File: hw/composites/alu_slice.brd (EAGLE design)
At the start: 50 x 50 mm, 7 parts, among them CON2 GENERIC-2X10

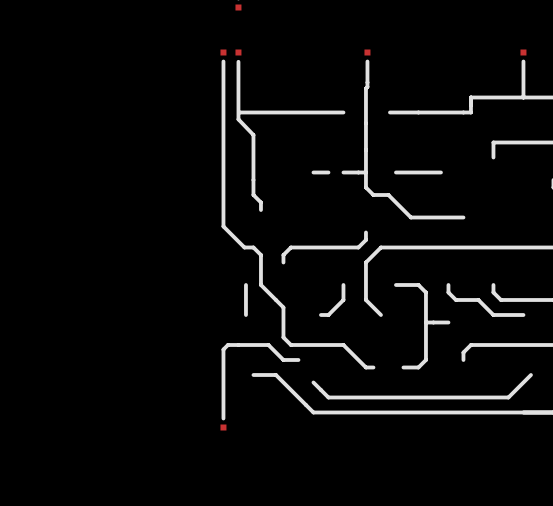
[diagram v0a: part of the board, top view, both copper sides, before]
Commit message: adds support for logical OR
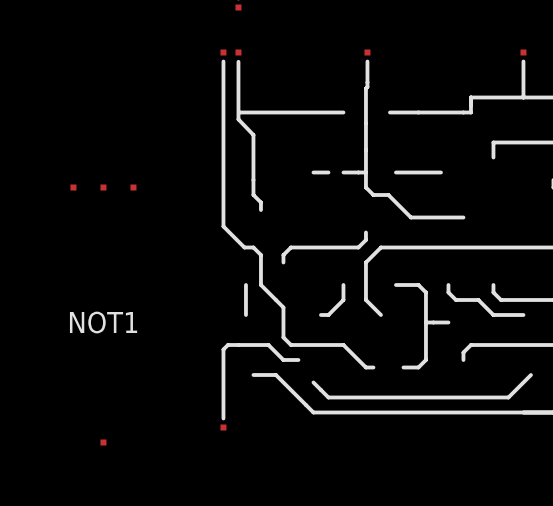
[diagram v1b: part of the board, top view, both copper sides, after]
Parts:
- added NOT1: NOTVERTICAL, p.peter-gator:NOT-VERTICAL
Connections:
- new net N$3: NOT1.NOT, SEL2.I7
- net +5V: now also NOT1._VP
- net GND: now also NOT1._VN
- net NOR: now also NOT1.A; no longer SEL2.I7
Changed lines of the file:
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@@
 <element name="XOR1" library="p.peter-gator" package="XOR" value="XOR" x="0.5" y="-20"/>
 <element name="XOR4" library="p.peter-gator" package="XOR" value="XOR" x="0" y="-34"/>
+<element name="NOT1" library="p.peter-gator" package="NOT-VERTICAL" value="NOTVERTICAL" x="-5.5" y="-34.5"/>
 </elements>
 <signals>
@@
 <contactref element="XOR1" pad="_VP"/>
 <contactref element="XOR4" pad="_VP"/>
+<contactref element="NOT1" pad="_VP"/>
 <wire x1="37.5" y1="34.5" x2="48.5" y2="32" width="0" layer="19" extent="1-1"/>
 <wire x1="15.5" y1="32" x2="37.5" y2="34.5" width="0" layer="19" extent="1-1"/>
 <wire x1="48" y1="5" x2="48.5" y2="32" width="0" layer="19" extent="1-1"/>
-<wire x1="17.07" y1="1.27" x2="48" y2="5" width="0" layer="19" extent="1-16"/>
-<wire x1="1.5" y1="-7.5" x2="17.07" y2="1.27" width="0" layer="19" extent="1-16"/>
+<wire x1="17.07" y1="1.27" x2="15.5" y2="32" width="0" layer="19" extent="1-1"/>
+<wire x1="1.5" y1="-7.5" x2="17.07" y2="1.27" width="0" layer="19" extent="1-1"/>
 <wire x1="1" y1="-21.5" x2="1.5" y2="-7.5" width="0" layer="19" extent="1-1"/>
+<wire x1="-2.5" y1="-26" x2="1" y2="-21.5" width="0" layer="19" extent="1-1"/>
 </signal>
 <signal name="GND">
@@
 <contactref element="XOR1" pad="_VN"/>
 <contactref element="XOR4" pad="_VN"/>
+<contactref element="NOT1" pad="_VN"/>
 <wire x1="27.8" y1="32" x2="47.5" y2="32" width="0" layer="19" extent="1-1"/>
 <wire x1="25.2" y1="34.5" x2="27.8" y2="32" width="0" layer="19" extent="1-1"/>
@@
 <wire x1="13.8" y1="-7.5" x2="39.93" y2="1.27" width="0" layer="19" extent="1-1"/>
 <wire x1="13.3" y1="-21.5" x2="13.8" y2="-7.5" width="0" layer="19" extent="1-1"/>
+<wire x1="-3.5" y1="-26" x2="13.3" y2="-21.5" width="0" layer="19" extent="1-1"/>
 </signal>
 <signal name="NOR">
 <contactref element="XOR2" pad="NOR"/>
-<contactref element="SEL2" pad="I7"/>
-<wire x1="39.8" y1="5" x2="33.2" y2="34.5" width="0" layer="19" extent="1-1"/>
+<contactref element="NOT1" pad="A"/>
+<wire x1="-3.5" y1="-34.5" x2="33.2" y2="34.5" width="0" layer="19" extent="1-1"/>
 </signal>
 <signal name="B">
@@
 <wire x1="27.23" y1="1.27" x2="0.5" y2="-34" width="0" layer="19" extent="1-16"/>
 </signal>
+<signal name="N$3">
+<contactref element="SEL2" pad="I7"/>
+<contactref element="NOT1" pad="NOT"/>
+<wire x1="-4.5" y1="-26" x2="39.8" y2="5" width="0" layer="19" extent="1-1"/>
+</signal>
 </signals>

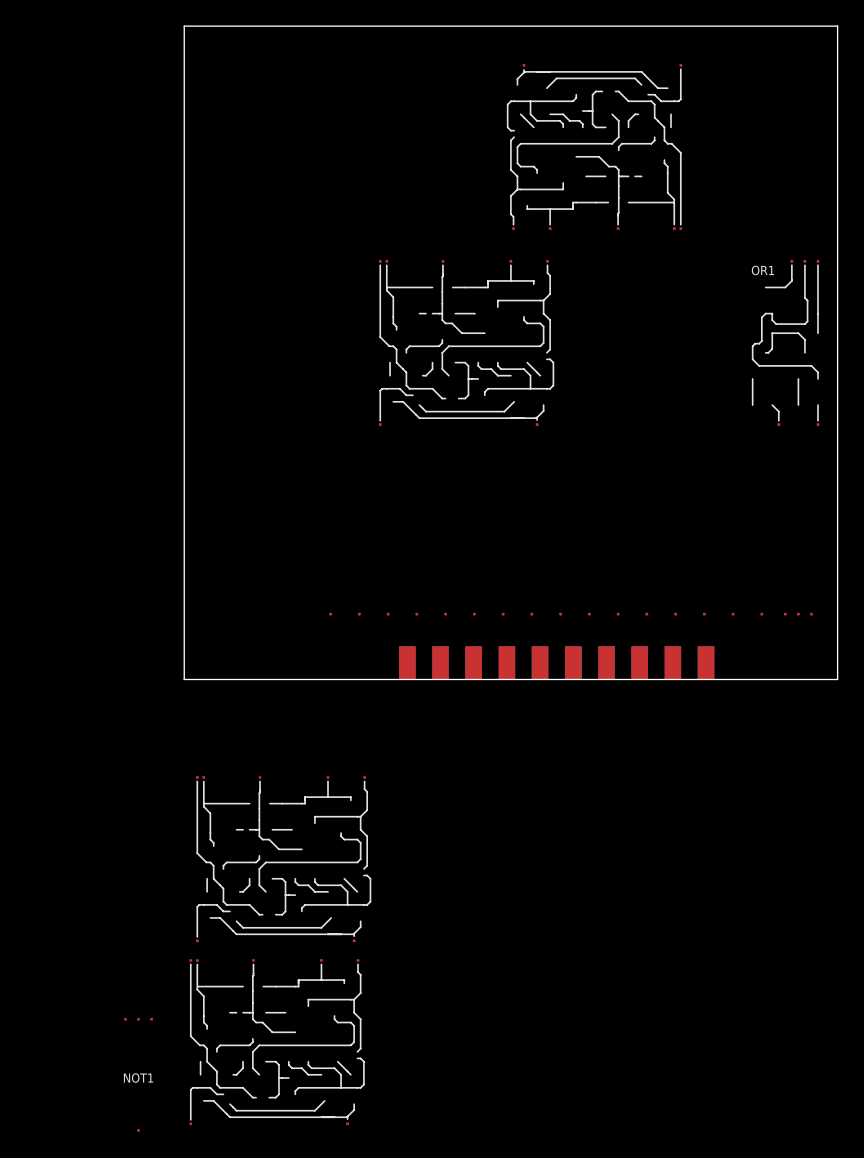
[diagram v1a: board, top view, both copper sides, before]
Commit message: adds support for bit shifts
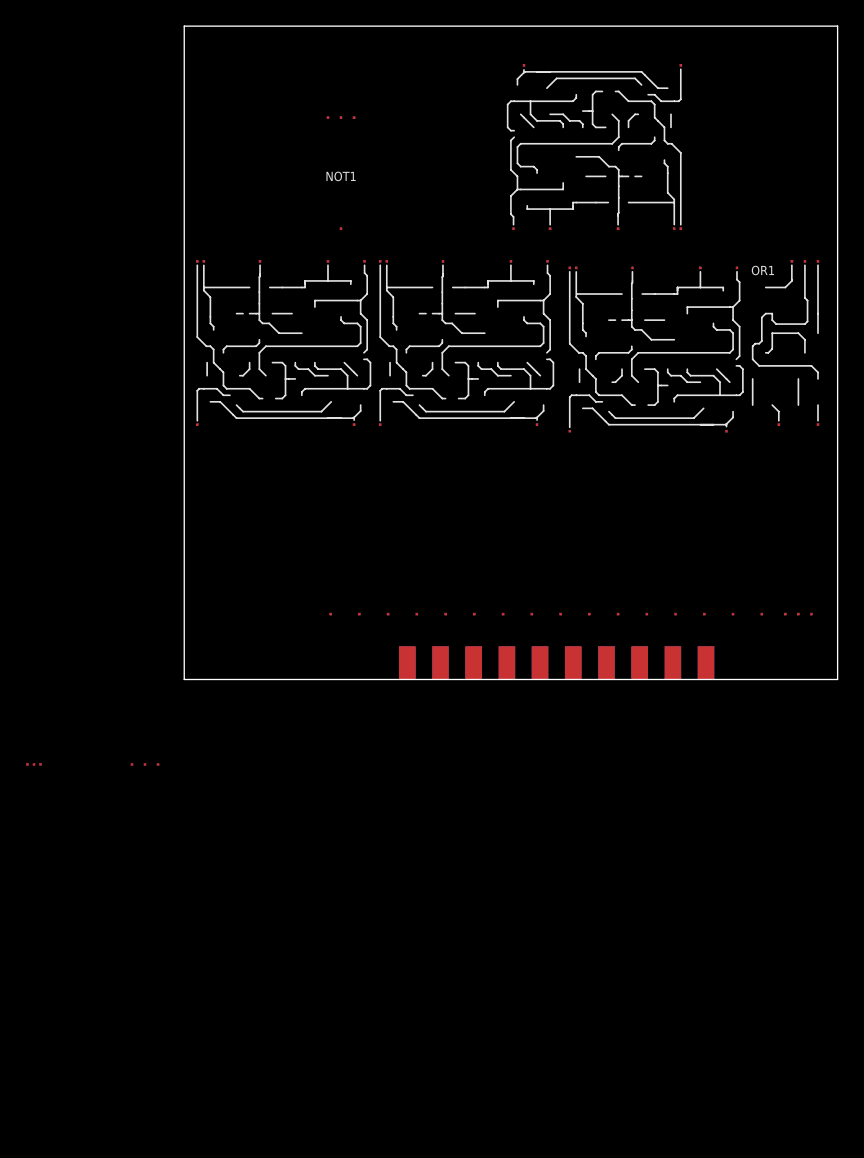
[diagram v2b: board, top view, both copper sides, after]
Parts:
- added SEL1: 1_BIT_SELECT, p.peter-gator:SELECTOR-2-LANE-NOMUX
- moved NOT1 70.7 mm to (10.0, 34.5)
- moved XOR4 60.4 mm to (29.0, 19.0)
- moved XOR1 39.5 mm to (0.50, 19.5)
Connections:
- new net N$5: SEL1.OUT, SEL2.I1
- new net RIGHT_IN: CON2.11, SEL1.A
- net +5V: now also SEL1._VP
- net CARRY_IN: now also SEL1.B
- net GND: now also SEL1._VN
- net LEFT_IN: no longer SEL2.I1
- net NC: no longer CON2.10, CON2.11, CON2.12, CON2.14
- net SUBTRACT: now also SEL1.SEL
- net S_OR: now also CON2.10
- net S_SHIFT: now also CON2.14
- net S_XOR: now also CON2.12
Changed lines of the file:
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@@
 <element name="SEL2" library="p.peter-gator" package="SELECTOR-8_BIT-NOMUX" value="8_BIT_SELECT" x="10" y="5"/>
 <element name="CON2" library="p.peter-connectors" package="PINHEADER-100MIL-2X10-EDGE" value="GENERIC-2X10" x="28.5" y="0"/>
-<element name="XOR1" library="p.peter-gator" package="XOR" value="XOR" x="0.5" y="-20"/>
-<element name="XOR4" library="p.peter-gator" package="XOR" value="XOR" x="0" y="-34"/>
-<element name="NOT1" library="p.peter-gator" package="NOT-VERTICAL" value="NOTVERTICAL" x="-5.5" y="-34.5"/>
+<element name="XOR1" library="p.peter-gator" package="XOR" value="XOR" x="0.5" y="19.5"/>
+<element name="XOR4" library="p.peter-gator" package="XOR" value="XOR" x="29" y="19"/>
+<element name="NOT1" library="p.peter-gator" package="NOT-VERTICAL" value="NOTVERTICAL" x="10" y="34.5"/>
+<element name="SEL1" library="p.peter-gator" package="SELECTOR-2-LANE-NOMUX" value="1_BIT_SELECT" x="-13" y="-6.5"/>
 </elements>
 <signals>
@@
 <contactref element="XOR3" pad="A"/>
 <contactref element="CON2" pad="5"/>
+<contactref element="SEL1" pad="B"/>
 <wire x1="22.15" y1="1.27" x2="27" y2="19.5" width="0" layer="19" extent="1-16"/>
+<wire x1="-11.5" y1="-6.5" x2="22.15" y2="1.27" width="0" layer="19" extent="1-16"/>
 </signal>
 <signal name="SUM">
@@
 <contactref element="XOR4" pad="_VP"/>
 <contactref element="NOT1" pad="_VP"/>
+<contactref element="SEL1" pad="_VP"/>
 <wire x1="37.5" y1="34.5" x2="48.5" y2="32" width="0" layer="19" extent="1-1"/>
-<wire x1="15.5" y1="32" x2="37.5" y2="34.5" width="0" layer="19" extent="1-1"/>
+<wire x1="30" y1="31.5" x2="37.5" y2="34.5" width="0" layer="19" extent="1-1"/>
+<wire x1="15.5" y1="32" x2="30" y2="31.5" width="0" layer="19" extent="1-1"/>
+<wire x1="13" y1="43" x2="15.5" y2="32" width="0" layer="19" extent="1-1"/>
+<wire x1="1.5" y1="32" x2="15.5" y2="32" width="0" layer="19" extent="1-1"/>
 <wire x1="48" y1="5" x2="48.5" y2="32" width="0" layer="19" extent="1-1"/>
 <wire x1="17.07" y1="1.27" x2="15.5" y2="32" width="0" layer="19" extent="1-1"/>
-<wire x1="1.5" y1="-7.5" x2="17.07" y2="1.27" width="0" layer="19" extent="1-1"/>
-<wire x1="1" y1="-21.5" x2="1.5" y2="-7.5" width="0" layer="19" extent="1-1"/>
-<wire x1="-2.5" y1="-26" x2="1" y2="-21.5" width="0" layer="19" extent="1-1"/>
+<wire x1="-2" y1="-6.5" x2="17.07" y2="1.27" width="0" layer="19" extent="1-1"/>
 </signal>
 <signal name="GND">
@@
 <contactref element="XOR4" pad="_VN"/>
 <contactref element="NOT1" pad="_VN"/>
-<wire x1="27.8" y1="32" x2="47.5" y2="32" width="0" layer="19" extent="1-1"/>
+<contactref element="SEL1" pad="_VN"/>
+<wire x1="42.3" y1="31.5" x2="47.5" y2="32" width="0" layer="19" extent="1-1"/>
+<wire x1="27.8" y1="32" x2="42.3" y2="31.5" width="0" layer="19" extent="1-1"/>
 <wire x1="25.2" y1="34.5" x2="27.8" y2="32" width="0" layer="19" extent="1-1"/>
-<wire x1="46" y1="5" x2="47.5" y2="32" width="0" layer="19" extent="1-1"/>
+<wire x1="13.8" y1="32" x2="25.2" y2="34.5" width="0" layer="19" extent="1-1"/>
+<wire x1="12" y1="43" x2="13.8" y2="32" width="0" layer="19" extent="1-1"/>
+<wire x1="46" y1="5" x2="42.3" y2="31.5" width="0" layer="19" extent="1-1"/>
 <wire x1="39.93" y1="1.27" x2="46" y2="5" width="0" layer="19" extent="1-1"/>
-<wire x1="13.8" y1="-7.5" x2="39.93" y2="1.27" width="0" layer="19" extent="1-1"/>
-<wire x1="13.3" y1="-21.5" x2="13.8" y2="-7.5" width="0" layer="19" extent="1-1"/>
-<wire x1="-3.5" y1="-26" x2="13.3" y2="-21.5" width="0" layer="19" extent="1-1"/>
+<wire x1="-4" y1="-6.5" x2="13.8" y2="32" width="0" layer="19" extent="1-1"/>
 </signal>
 <signal name="NOR">
 <contactref element="XOR2" pad="NOR"/>
 <contactref element="NOT1" pad="A"/>
-<wire x1="-3.5" y1="-34.5" x2="33.2" y2="34.5" width="0" layer="19" extent="1-1"/>
+<wire x1="12" y1="34.5" x2="33.2" y2="34.5" width="0" layer="19" extent="1-1"/>
 </signal>
 <signal name="B">
@@
 <contactref element="CON2" pad="3"/>
 <contactref element="XOR4" pad="A"/>
-<wire x1="19.61" y1="1.27" x2="12.5" y2="-34" width="0" layer="19" extent="1-16"/>
+<wire x1="19.61" y1="1.27" x2="41.5" y2="19" width="0" layer="19" extent="1-16"/>
 <wire x1="17.8" y1="5" x2="19.61" y2="1.27" width="0" layer="19" extent="1-16"/>
 </signal>
 <signal name="LEFT_IN">
 <contactref element="SEL2" pad="I3"/>
-<contactref element="SEL2" pad="I1"/>
-<wire x1="13.4" y1="5" x2="22.2" y2="5" width="0" layer="19" extent="1-1"/>
 </signal>
 <signal name="AND">
@@
 <signal name="S_OR">
 <contactref element="SEL2" pad="S7"/>
+<contactref element="CON2" pad="10"/>
+<wire x1="27.23" y1="1.27" x2="37.6" y2="5" width="0" layer="19" extent="1-1"/>
 </signal>
 <signal name="S_XOR">
 <contactref element="SEL2" pad="S6"/>
+<contactref element="CON2" pad="12"/>
+<wire x1="29.77" y1="1.27" x2="33.2" y2="5" width="0" layer="19" extent="1-1"/>
 </signal>
 <signal name="S_ADD">
@@
 <signal name="S_SHIFT">
 <contactref element="SEL2" pad="S1"/>
+<contactref element="CON2" pad="14"/>
+<wire x1="11.2" y1="5" x2="32.31" y2="1.27" width="0" layer="19" extent="1-1"/>
 </signal>
 <signal name="RESULT">
 <contactref element="CON2" pad="19"/>
 <contactref element="XOR1" pad="XOR"/>
-<wire x1="11" y1="-7.5" x2="39.93" y2="1.27" width="0" layer="19" extent="1-16"/>
+<wire x1="11" y1="32" x2="39.93" y2="1.27" width="0" layer="19" extent="1-16"/>
 </signal>
 <signal name="N$4">
 </signal>
 <signal name="NC">
-<contactref element="CON2" pad="11"/>
 <contactref element="CON2" pad="13"/>
 <contactref element="CON2" pad="15"/>
-<contactref element="CON2" pad="10"/>
-<contactref element="CON2" pad="12"/>
-<contactref element="CON2" pad="14"/>
 <contactref element="CON2" pad="16"/>
 <contactref element="CON2" pad="18"/>
-<wire x1="34.85" y1="1.27" x2="37.39" y2="1.27" width="0" layer="19" extent="1-1"/>
-<wire x1="32.31" y1="1.27" x2="34.85" y2="1.27" width="0" layer="19" extent="1-16"/>
-<wire x1="32.31" y1="1.27" x2="32.31" y2="1.27" width="0" layer="19" extent="1-16"/>
-<wire x1="29.77" y1="1.27" x2="32.31" y2="1.27" width="0" layer="19" extent="16-16"/>
-<wire x1="29.77" y1="1.27" x2="29.77" y2="1.27" width="0" layer="19" extent="1-16"/>
-<wire x1="27.23" y1="1.27" x2="29.77" y2="1.27" width="0" layer="19" extent="1-16"/>
-<wire x1="34.85" y1="1.27" x2="27.23" y2="1.27" width="0" layer="19" extent="1-1"/>
+<wire x1="34.85" y1="1.27" x2="37.39" y2="1.27" width="0" layer="19" extent="1-16"/>
+<wire x1="34.85" y1="1.27" x2="34.85" y2="1.27" width="0" layer="19" extent="1-16"/>
+<wire x1="32.31" y1="1.27" x2="34.85" y2="1.27" width="0" layer="19" extent="16-16"/>
 </signal>
 <signal name="INVERT_OUT">
 <contactref element="CON2" pad="7"/>
 <contactref element="XOR1" pad="B"/>
-<wire x1="1" y1="-20" x2="24.69" y2="1.27" width="0" layer="19" extent="1-16"/>
+<wire x1="1" y1="19.5" x2="24.69" y2="1.27" width="0" layer="19" extent="1-16"/>
 </signal>
 <signal name="N$1">
 <contactref element="SEL2" pad="OUT"/>
 <contactref element="XOR1" pad="A"/>
-<wire x1="13" y1="-20" x2="47" y2="5" width="0" layer="19" extent="1-1"/>
+<wire x1="13" y1="19.5" x2="47" y2="5" width="0" layer="19" extent="1-1"/>
 </signal>
 <signal name="N$2">
 <contactref element="XOR2" pad="B"/>
 <contactref element="XOR4" pad="XOR"/>
-<wire x1="10.5" y1="-21.5" x2="38" y2="47" width="0" layer="19" extent="1-1"/>
+<wire x1="39.5" y1="31.5" x2="38" y2="47" width="0" layer="19" extent="1-1"/>
 </signal>
 <signal name="SUBTRACT">
 <contactref element="XOR4" pad="B"/>
 <contactref element="CON2" pad="9"/>
-<wire x1="27.23" y1="1.27" x2="0.5" y2="-34" width="0" layer="19" extent="1-16"/>
+<contactref element="SEL1" pad="SEL"/>
+<wire x1="27.23" y1="1.27" x2="29.5" y2="19" width="0" layer="19" extent="1-16"/>
+<wire x1="-11" y1="-6.5" x2="27.23" y2="1.27" width="0" layer="19" extent="1-16"/>
 </signal>
 <signal name="N$3">
 <contactref element="SEL2" pad="I7"/>
 <contactref element="NOT1" pad="NOT"/>
-<wire x1="-4.5" y1="-26" x2="39.8" y2="5" width="0" layer="19" extent="1-1"/>
+<wire x1="11" y1="43" x2="39.8" y2="5" width="0" layer="19" extent="1-1"/>
+</signal>
+<signal name="RIGHT_IN">
+<contactref element="CON2" pad="11"/>
+<contactref element="SEL1" pad="A"/>
+<wire x1="-12" y1="-6.5" x2="29.77" y2="1.27" width="0" layer="19" extent="1-16"/>
+</signal>
+<signal name="N$5">
+<contactref element="SEL2" pad="I1"/>
+<contactref element="SEL1" pad="OUT"/>
+<wire x1="-3" y1="-6.5" x2="13.4" y2="5" width="0" layer="19" extent="1-1"/>
 </signal>
 </signals>

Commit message: Separated input for shift from inputs for addition
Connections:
- removed net LEFT_IN: SEL2.I3
- removed net RIGHT_IN: CON2.11, SEL1.A
- new net LEFT_A: CON2.11, SEL1.B
- new net RIGHT_A: CON2.13, SEL1.A
- net A: now also SEL2.I3
- net CARRY_IN: no longer SEL1.B
- net NC: no longer CON2.13
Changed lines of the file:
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@@
 <contactref element="SEL2" pad="I4"/>
 <contactref element="CON2" pad="1"/>
+<contactref element="SEL2" pad="I3"/>
 <wire x1="26.6" y1="5" x2="26" y2="47" width="0" layer="19" extent="1-1"/>
-<wire x1="17.07" y1="1.27" x2="26.6" y2="5" width="0" layer="19" extent="1-16"/>
+<wire x1="22.2" y1="5" x2="26.6" y2="5" width="0" layer="19" extent="1-1"/>
+<wire x1="17.07" y1="1.27" x2="22.2" y2="5" width="0" layer="19" extent="1-16"/>
 </signal>
 <signal name="XOR">
@@
 <contactref element="XOR3" pad="A"/>
 <contactref element="CON2" pad="5"/>
-<contactref element="SEL1" pad="B"/>
 <wire x1="22.15" y1="1.27" x2="27" y2="19.5" width="0" layer="19" extent="1-16"/>
-<wire x1="-11.5" y1="-6.5" x2="22.15" y2="1.27" width="0" layer="19" extent="1-16"/>
 </signal>
 <signal name="SUM">
@@
 <wire x1="17.8" y1="5" x2="19.61" y2="1.27" width="0" layer="19" extent="1-16"/>
 </signal>
-<signal name="LEFT_IN">
-<contactref element="SEL2" pad="I3"/>
-</signal>
 <signal name="AND">
 <contactref element="OR1" pad="B"/>
@@
 </signal>
 <signal name="NC">
-<contactref element="CON2" pad="13"/>
 <contactref element="CON2" pad="15"/>
 <contactref element="CON2" pad="16"/>
@@
 <wire x1="34.85" y1="1.27" x2="37.39" y2="1.27" width="0" layer="19" extent="1-16"/>
 <wire x1="34.85" y1="1.27" x2="34.85" y2="1.27" width="0" layer="19" extent="1-16"/>
-<wire x1="32.31" y1="1.27" x2="34.85" y2="1.27" width="0" layer="19" extent="16-16"/>
 </signal>
 <signal name="INVERT_OUT">
@@
 <wire x1="11" y1="43" x2="39.8" y2="5" width="0" layer="19" extent="1-1"/>
 </signal>
-<signal name="RIGHT_IN">
-<contactref element="CON2" pad="11"/>
-<contactref element="SEL1" pad="A"/>
-<wire x1="-12" y1="-6.5" x2="29.77" y2="1.27" width="0" layer="19" extent="1-16"/>
-</signal>
 <signal name="N$5">
 <contactref element="SEL2" pad="I1"/>
@@
 <wire x1="-3" y1="-6.5" x2="13.4" y2="5" width="0" layer="19" extent="1-1"/>
 </signal>
+<signal name="RIGHT_A">
+<contactref element="SEL1" pad="A"/>
+<contactref element="CON2" pad="13"/>
+<wire x1="-12" y1="-6.5" x2="32.31" y2="1.27" width="0" layer="19" extent="1-16"/>
+</signal>
+<signal name="LEFT_A">
+<contactref element="SEL1" pad="B"/>
+<contactref element="CON2" pad="11"/>
+<wire x1="-11.5" y1="-6.5" x2="29.77" y2="1.27" width="0" layer="19" extent="1-16"/>
+</signal>
 </signals>
